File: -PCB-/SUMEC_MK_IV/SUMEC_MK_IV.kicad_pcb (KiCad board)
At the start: 2 copper layers, 15 parts, among them U1 TPS62133, U2 ESP32-S3-WROOM-1, U3 ESP32-S3-WROOM-1

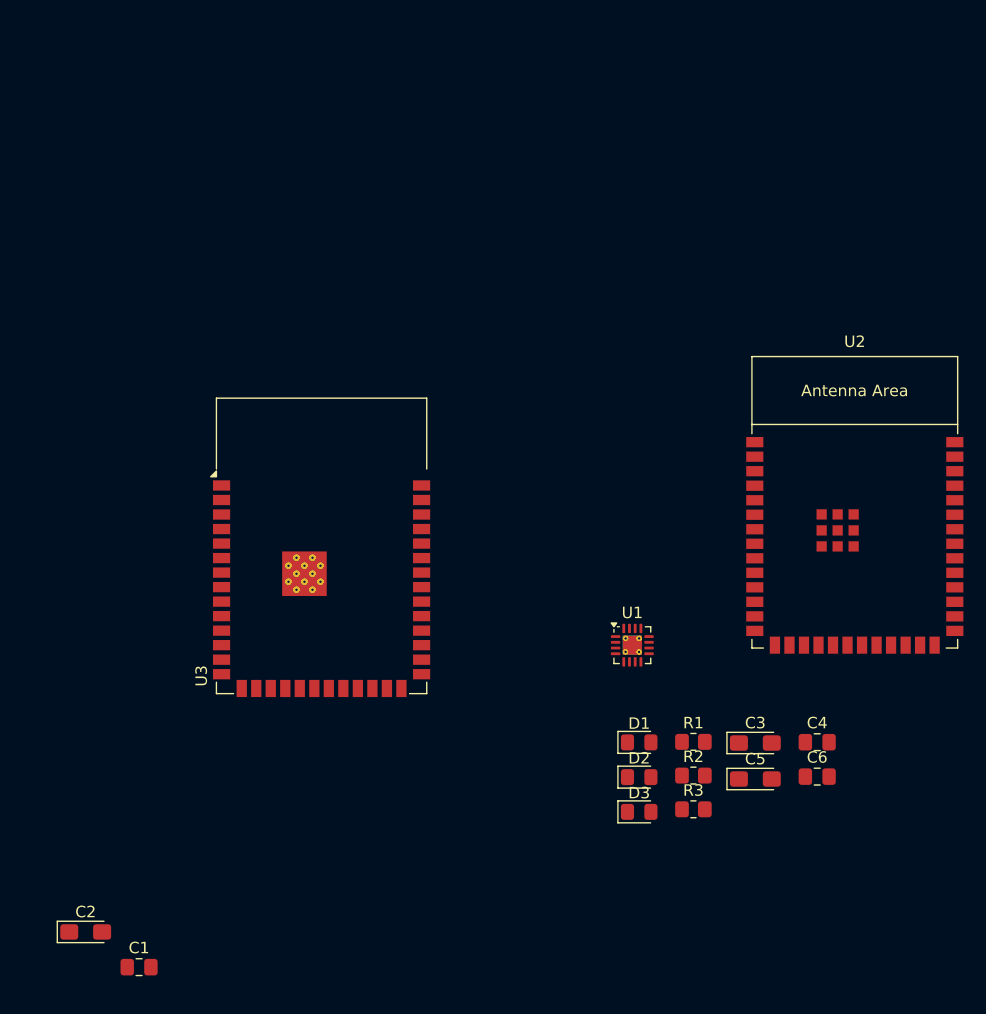
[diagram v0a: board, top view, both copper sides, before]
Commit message: VBATT VBUS Switching
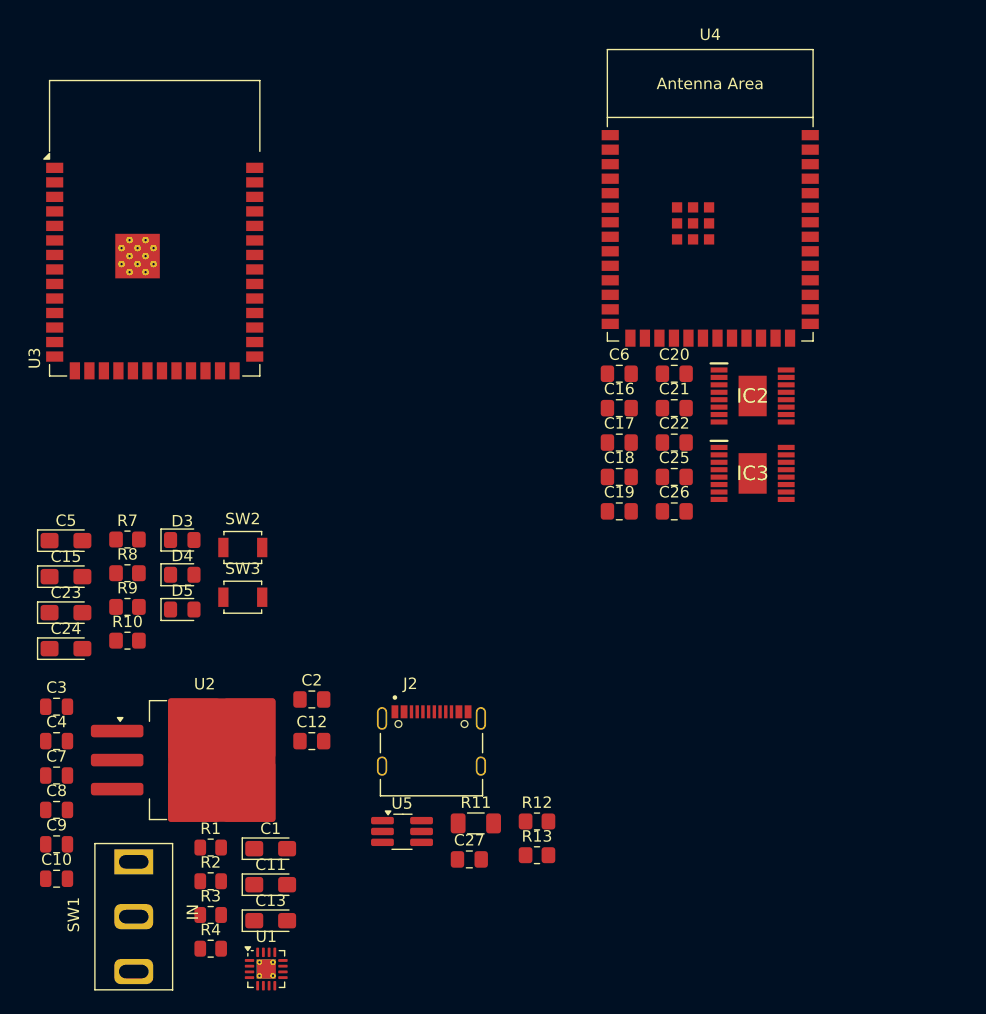
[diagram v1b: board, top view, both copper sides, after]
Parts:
- removed D1, D2: LED, LED_SMD:LED_0805_2012Metric_Pad1.15x1.40mm_HandSolder
- added C10: 100nF, Capacitor_SMD:C_0805_2012Metric, F.Cu at (111.7, 100.9)
- added C11: 10uF.stabl, Capacitor_Tantalum_SMD:CP_EIA-3216-18_Kemet-A_Pad1.58x1.35mm_HandSolder, F.Cu at (130.4, 101.5)
- added C12: 3.3nF, Capacitor_SMD:C_0805_2012Metric_Pad1.18x1.45mm_HandSolder, F.Cu at (134.0, 88.9)
- added C13: 10uF.stabl, Capacitor_Tantalum_SMD:CP_EIA-3216-18_Kemet-A_Pad1.58x1.35mm_HandSolder, F.Cu at (130.4, 104.6)
- added C15: 10uF.mcu, Capacitor_Tantalum_SMD:CP_EIA-3216-18_Kemet-A_Pad1.58x1.35mm_HandSolder, F.Cu at (112.5, 74.5)
- added C16: 100nF.mcu, Capacitor_SMD:C_0805_2012Metric_Pad1.18x1.45mm_HandSolder, F.Cu at (160.9, 59.8)
- added C17: 22nF.hb, Capacitor_SMD:C_0805_2012Metric_Pad1.18x1.45mm_HandSolder, F.Cu at (160.9, 62.8)
- added C18: 22nF.hb, Capacitor_SMD:C_0805_2012Metric_Pad1.18x1.45mm_HandSolder, F.Cu at (160.9, 65.8)
- added C19: 100nF, Capacitor_SMD:C_0805_2012Metric_Pad1.18x1.45mm_HandSolder, F.Cu at (160.9, 68.8)
- added C20: 100nF, Capacitor_SMD:C_0805_2012Metric_Pad1.18x1.45mm_HandSolder, F.Cu at (165.7, 56.8)
- added C21: 100nF.hb, Capacitor_SMD:C_0805_2012Metric_Pad1.18x1.45mm_HandSolder, F.Cu at (165.7, 59.8)
- added C22: 100nF.hb, Capacitor_SMD:C_0805_2012Metric_Pad1.18x1.45mm_HandSolder, F.Cu at (165.7, 62.8)
- added C23: 10uF.hb, Capacitor_Tantalum_SMD:CP_EIA-3216-18_Kemet-A_Pad1.58x1.35mm_HandSolder, F.Cu at (112.5, 77.7)
- added C24: 10uF.hb, Capacitor_Tantalum_SMD:CP_EIA-3216-18_Kemet-A_Pad1.58x1.35mm_HandSolder, F.Cu at (112.5, 80.8)
- added C25: 100nF.en, Capacitor_SMD:C_0805_2012Metric_Pad1.18x1.45mm_HandSolder, F.Cu at (165.7, 65.8)
- added C26: 100nF.boot, Capacitor_SMD:C_0805_2012Metric_Pad1.18x1.45mm_HandSolder, F.Cu at (165.7, 68.8)
- added C27: 100nF, Capacitor_SMD:C_0805_2012Metric_Pad1.18x1.45mm_HandSolder, F.Cu at (147.8, 99.2)
- added C7: 22uF, Capacitor_SMD:C_0805_2012Metric, F.Cu at (111.7, 91.9)
- added C8: 22uF, Capacitor_SMD:C_0805_2012Metric, F.Cu at (111.7, 94.9)
- added C9: 22uF, Capacitor_SMD:C_0805_2012Metric, F.Cu at (111.7, 97.9)
- added D4: LED, LED_SMD:LED_0805_2012Metric_Pad1.15x1.40mm_HandSolder, F.Cu at (122.7, 74.3)
- added D5: LED, LED_SMD:LED_0805_2012Metric_Pad1.15x1.40mm_HandSolder, F.Cu at (122.7, 77.4)
- added IC2: DRV8874PWPR, sumec-smdV2_library:DRV8874, F.Cu at (172.6, 58.7)
- added IC3: DRV8874PWPR, sumec-smdV2_library:DRV8874, F.Cu at (172.6, 65.5)
- added J2: TYPE-C-31-M-12, sumec-smdV2_library:USB_Type_C, F.Cu at (144.5, 91.1)
- added R10: 10k.mcu, Resistor_SMD:R_0805_2012Metric_Pad1.20x1.40mm_HandSolder, F.Cu at (117.9, 80.1)
- added R11: 0R, Resistor_SMD:R_1206_3216Metric_Pad1.30x1.75mm_HandSolder, F.Cu at (148.3, 96.1)
- added R12: 15R, Resistor_SMD:R_0805_2012Metric_Pad1.20x1.40mm_HandSolder, F.Cu at (153.7, 95.9)
- added R13: 15R, Resistor_SMD:R_0805_2012Metric_Pad1.20x1.40mm_HandSolder, F.Cu at (153.7, 98.9)
- added R4: 33k, Resistor_SMD:R_0805_2012Metric, F.Cu at (125.1, 107.1)
- added R7: 100R, Resistor_SMD:R_0805_2012Metric_Pad1.20x1.40mm_HandSolder, F.Cu at (117.9, 71.3)
- added R8: 100R, Resistor_SMD:R_0805_2012Metric_Pad1.20x1.40mm_HandSolder, F.Cu at (117.9, 74.2)
- added R9: 560R, Resistor_SMD:R_0805_2012Metric_Pad1.20x1.40mm_HandSolder, F.Cu at (117.9, 77.2)
- added SW1: SW_DPDT_x2, sumec-smdV2_library:Custom_SPDT_4.8mm_Switch, F.Cu at (118.4, 104.2)
- added SW2: SW_Push, Button_Switch_SMD:SW_SPST_B3U-1000P, F.Cu at (128.0, 72.0)
- added SW3: SW_Push, Button_Switch_SMD:SW_SPST_B3U-1000P, F.Cu at (128.0, 76.3)
- added U4: ESP32-S3-WROOM-1, PCM_Espressif:ESP32-S3-WROOM-1, F.Cu at (168.9, 44.1)
- added U5: USBLC6-2SC6, Package_TO_SOT_SMD:TSOT-23-6_HandSoldering, F.Cu at (141.9, 96.8)
- C1: value 100nF.mcu -> 10uF.bck; footprint Capacitor_SMD:C_0805_2012Metric_Pad1.18x1.45mm_HandSolder -> Capacitor_Tantalum_SMD:CP_EIA-3216-18_Kemet-A_Pad1.58x1.35mm_HandSolder
- C2: value 10uF.mcu -> 100nF.bck; footprint Capacitor_Tantalum_SMD:CP_EIA-3216-18_Kemet-A_Pad1.58x1.35mm_HandSolder -> Capacitor_SMD:C_0805_2012Metric_Pad1.18x1.45mm_HandSolder
- C3: value 10uF.mcu -> 22uF; footprint Capacitor_Tantalum_SMD:CP_EIA-3216-18_Kemet-A_Pad1.58x1.35mm_HandSolder -> Capacitor_SMD:C_0805_2012Metric
- C4: value 100nF.mcu -> 100nF; footprint Capacitor_SMD:C_0805_2012Metric_Pad1.18x1.45mm_HandSolder -> Capacitor_SMD:C_0805_2012Metric
- R1: value 100R -> 100k; footprint Resistor_SMD:R_0805_2012Metric_Pad1.20x1.40mm_HandSolder -> Resistor_SMD:R_0805_2012Metric
- R2: value 100R -> 22k; footprint Resistor_SMD:R_0805_2012Metric_Pad1.20x1.40mm_HandSolder -> Resistor_SMD:R_0805_2012Metric
- R3: value 560R -> 150k; footprint Resistor_SMD:R_0805_2012Metric_Pad1.20x1.40mm_HandSolder -> Resistor_SMD:R_0805_2012Metric
- U2: value ESP32-S3-WROOM-1 -> LM1084-3.3; footprint PCM_Espressif:ESP32-S3-WROOM-1 -> Package_TO_SOT_SMD:TO-263-3_TabPin2
- moved C4 66.5 mm to (111.7, 88.9)
- moved C5 63.8 mm to (112.5, 71.4)
- moved C3 61.2 mm to (111.7, 85.9)
- moved U2 60.2 mm to (124.6, 90.6)
- moved D3 46.5 mm to (122.7, 71.3)
- moved R1 43.2 mm to (125.1, 98.2)
- moved R2 43.2 mm to (125.1, 101.2)
- moved R3 43.2 mm to (125.1, 104.1)
- moved U1 42.8 mm to (130.0, 108.8)
- moved C6 39.3 mm to (160.9, 56.8)
- moved U3 31.4 mm to (120.2, 44.0)
- moved C2 28.4 mm to (134.0, 85.2)
- moved C1 15.5 mm to (130.4, 98.3)
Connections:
- C1 pad 1: unconnected-(C1-Pad1) -> +12V
- C1 pad 2: unconnected-(C1-Pad2) -> GND
- C2 pad 1: unconnected-(C2-Pad1) -> +12V
- C2 pad 2: unconnected-(C2-Pad2) -> GND
- C3 pad 1: +3V3 -> +BATT
- C4 pad 1: +3V3 -> +BATT
- D3 pad 2: +12V -> LED1
- R1 pad 1: Net-(D1-K) -> +BATT
- R1 pad 2: GND -> /POWER_SUPPLY/En_3V3
- R2 pad 1: Net-(D2-K) -> /POWER_SUPPLY/En_3V3
- R3 pad 1: Net-(D3-K) -> VCC
- R3 pad 2: GND -> Net-(IC1-FB)
- U1 pad 10: Net-(U1-VIN-Pad10) -> +12V
- U1 pad 11: Net-(U1-VIN-Pad10) -> +12V
- U1 pad 12: Net-(U1-VIN-Pad10) -> +12V
- U1 pad 13: unconnected-(U1-EN-Pad13) -> +12V
- U1 pad 14: unconnected-(U1-VOS-Pad14) -> VOUT 5V
- U1 pad 15: Net-(U1-GND-Pad15) -> GND
- U1 pad 16: Net-(U1-GND-Pad15) -> GND
- U1 pad 17: Net-(U1-GND-Pad15) -> GND
- U1 pad 4: unconnected-(U1-PG-Pad4) -> Net-(U1-PG)
- U1 pad 5: unconnected-(U1-FB-Pad5) -> GND
- U1 pad 6: Net-(U1-GND-Pad15) -> GND
- U1 pad 7: unconnected-(U1-FSW-Pad7) -> GND
- U1 pad 8: unconnected-(U1-DEF-Pad8) -> GND
- U1 pad 9: unconnected-(U1-SS/TR-Pad9) -> Net-(U1-SS/TR)
- U2 pad 3: EN -> +5V

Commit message: MK_IV update
Power supp sheet done, mechanical sheet almost done, some changes, updates etc.
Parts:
- added C28: 10uF.shrp, Capacitor_Tantalum_SMD:CP_EIA-3216-18_Kemet-A_Pad1.58x1.35mm_HandSolder, F.Cu at (149.8, 85.1)
- added C29: 10uF.shrp, Capacitor_Tantalum_SMD:CP_EIA-3216-18_Kemet-A_Pad1.58x1.35mm_HandSolder, F.Cu at (149.8, 88.3)
- added H1: Mounting Hole M3, MountingHole:MountingHole_3.2mm_M3_Pad_Via, F.Cu at (126.8, 66.7)
- added H2: Mounting Hole M3, MountingHole:MountingHole_3.2mm_M3_Pad_Via, F.Cu at (126.8, 74.6)
- added H3: Mounting Hole M3, MountingHole:MountingHole_3.2mm_M3_Pad_Via, F.Cu at (126.8, 82.6)
- added H4: Mounting Hole M3, MountingHole:MountingHole_3.2mm_M3_Pad_Via, F.Cu at (126.8, 90.5)
- added J3: Conn_01x06_Pin, Connector_Molex:Molex_PicoBlade_53398-0671_1x06-1MP_P1.25mm_Vertical, F.Cu at (149.9, 65.6)
- added J4: Conn_01x06_Pin, Connector_Molex:Molex_PicoBlade_53398-0671_1x06-1MP_P1.25mm_Vertical, F.Cu at (149.9, 72.6)
- added J5: Conn_01x06_Pin, Connector_Molex:Molex_PicoBlade_53398-0671_1x06-1MP_P1.25mm_Vertical, F.Cu at (149.9, 79.5)
- added J6: Conn_01x03_Pin, Connector_Molex:Molex_PicoBlade_53398-0371_1x03-1MP_P1.25mm_Vertical, F.Cu at (163.6, 65.6)
- added J7: Conn_01x03_Pin, Connector_Molex:Molex_PicoBlade_53398-0371_1x03-1MP_P1.25mm_Vertical, F.Cu at (163.6, 72.6)
- added J8: Conn_01x04_Pin, Connector_Molex:Molex_PicoBlade_53398-0471_1x04-1MP_P1.25mm_Vertical, F.Cu at (164.2, 86.5)
- added J9: Conn_01x03_Pin, Connector_Molex:Molex_PicoBlade_53398-0371_1x03-1MP_P1.25mm_Vertical, F.Cu at (163.6, 79.5)
- added R14: 10k, Resistor_SMD:R_0805_2012Metric_Pad1.20x1.40mm_HandSolder, F.Cu at (155.2, 85.0)
- added R15: 100, Resistor_SMD:R_0805_2012Metric_Pad1.20x1.40mm_HandSolder, F.Cu at (155.2, 88.0)
- added R16: R, sumec-remote_library:purosidenegative, F.Cu at (74.4, 34.7)
- added R17: R, sumec-smdV2_library:SPS LOGO, F.Cu at (201.8, -44.1)
- added R18: R, sumec-remote_library:boi, F.Cu at (107.1, 29.8)
- added R19: R, sumec-smdV2_library:Logo, F.Cu at (143.9, 17.3)
- added SW4: SW_Push, Button_Switch_SMD:SW_SPST_B3U-1000P, F.Cu at (133.7, 73.6)
- added SW5: SW_Push, Button_Switch_SMD:SW_SPST_B3U-1000P, F.Cu at (133.7, 77.9)
- added SW6: SW_Push, Button_Switch_SMD:SW_SPST_B3U-1000P, F.Cu at (133.7, 82.3)
- added TP1: TestPoint, TestPoint:TestPoint_Pad_D1.5mm, F.Cu at (138.4, 64.5)
- added TP2: TestPoint, TestPoint:TestPoint_Pad_D1.5mm, F.Cu at (138.4, 68.0)
- added TP3: TestPoint, TestPoint:TestPoint_Pad_D1.5mm, F.Cu at (138.4, 71.6)
- added TP4: TestPoint, TestPoint:TestPoint_Pad_D1.5mm, F.Cu at (138.4, 75.1)
- added U6: TSOP382xx, sumec-smdV2_library:TSOP, F.Cu at (144.5, 85.9)
- C11, C13: value 10uF.stabl -> 10uF.reg
- C2: value 100nF.bck -> 100nF.avin
- moved C23 92.2 mm to (204.7, 77.8)
- moved C24 92.2 mm to (204.7, 81.0)
- moved C27 81.9 mm to (226.7, 77.6)
- moved J2 81.9 mm to (223.4, 69.4)
- moved R11 81.9 mm to (227.3, 74.4)
- moved R12 81.9 mm to (232.7, 74.3)
- moved R13 81.9 mm to (232.7, 77.2)
- moved U5 81.9 mm to (220.8, 75.1)
- moved U4 68.2 mm to (110.5, 79.3)
- moved C1 66.9 mm to (193.6, 76.6)
- moved C10 66.9 mm to (174.9, 79.3)
- moved C11 66.9 mm to (193.6, 79.8)
- moved C13 66.9 mm to (193.6, 82.9)
- moved C3 66.9 mm to (174.9, 64.2)
- moved C4 66.9 mm to (174.9, 67.2)
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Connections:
- net OUT 1A renamed M1A
- net OUT 1B renamed M1B
- net OUT 2A renamed M2A
- net OUT 2B renamed M2B
- C5 pad 1: Net-(U3-3V3) -> +3V3
- C6 pad 1: Net-(U3-3V3) -> +3V3
- U3 pad 13: unconnected-(U3-IO19-Pad13) -> D-
- U3 pad 14: unconnected-(U3-IO20-Pad14) -> D+
- U3 pad 2: Net-(U3-3V3) -> +3V3

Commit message: MKIV major update
Updated everything, custom symbol for ESP32, MCU sheet done, new test points added, motor control revision.

all left is to clean it up a bit
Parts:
- removed C17, C18: 22nF.hb, Capacitor_SMD:C_0805_2012Metric_Pad1.18x1.45mm_HandSolder
- removed C19, C20: 100nF, Capacitor_SMD:C_0805_2012Metric_Pad1.18x1.45mm_HandSolder
- added D7: LED, LED_SMD:LED_0805_2012Metric_Pad1.15x1.40mm_HandSolder, F.Cu at (91.5, 144.8)
- added R26: 0R, Resistor_SMD:R_1206_3216Metric_Pad1.30x1.75mm_HandSolder, F.Cu at (202.5, 108.1)
- added R27: 0R, Resistor_SMD:R_1206_3216Metric_Pad1.30x1.75mm_HandSolder, F.Cu at (202.5, 111.4)
- added R28: 0R, Resistor_SMD:R_1206_3216Metric_Pad1.30x1.75mm_HandSolder, F.Cu at (202.5, 114.7)
- added R29: 0R, Resistor_SMD:R_1206_3216Metric_Pad1.30x1.75mm_HandSolder, F.Cu at (202.5, 118.0)
- added R30: 100R, Resistor_SMD:R_0805_2012Metric_Pad1.20x1.40mm_HandSolder, F.Cu at (96.2, 144.5)
- added TP5: TestPoint, TestPoint:TestPoint_Pad_D1.5mm, F.Cu at (127.4, 118.9)
- added TP6: TestPoint, TestPoint:TestPoint_Pad_D1.5mm, F.Cu at (127.4, 122.4)
- J4: value Conn_01x06_Pin -> Conn_01x03_Pin; footprint Connector_Molex:Molex_PicoBlade_53398-0671_1x06-1MP_P1.25mm_Vertical -> Connector_Molex:Molex_PicoBlade_53398-0371_1x03-1MP_P1.25mm_Vertical
- J7: value Conn_01x03_Pin -> Conn_01x06_Pin; footprint Connector_Molex:Molex_PicoBlade_53398-0371_1x03-1MP_P1.25mm_Vertical -> Connector_Molex:Molex_PicoBlade_53398-0671_1x06-1MP_P1.25mm_Vertical
- TP1: footprint TestPoint:TestPoint_Pad_D1.5mm -> TestPoint:TestPoint_Loop_D1.80mm_Drill1.0mm_Beaded
- moved U2 96.6 mm to (138.7, 152.0)
- moved TP1 67.1 mm to (126.9, 130.5)
- moved J7 56.4 mm to (138.9, 123.3)
- moved R19 54.1 mm to (107.9, 57.8)
- moved J6 51.9 mm to (152.6, 116.3)
- moved C21 49.4 mm to (193.1, 121.5)
- moved C22 49.4 mm to (193.1, 124.5)
- moved C16 45.1 mm to (107.1, 138.7)
- moved C26 45.1 mm to (122.1, 132.7)
- moved D3 45.1 mm to (91.5, 135.7)
- moved R8 45.1 mm to (96.2, 138.6)
- moved H1 45.1 mm to (115.8, 110.4)
- moved H2 45.1 mm to (115.8, 118.4)
- moved H3 45.1 mm to (115.8, 126.3)
- moved R10 45.1 mm to (122.1, 135.7)
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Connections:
- C3 pad 1: +BATT -> +5V
- C4 pad 1: +BATT -> +5V
- IC2 pad 16: GND -> Net-(IC2-PMODE)
- IC2 pad 4: unconnected-(IC2-NFAULT-Pad4) -> nFAULT
- IC2 pad 5: unconnected-(IC2-VREF-Pad5) -> +3V3
- IC2 pad 6: unconnected-(IC2-IPROPI-Pad6) -> IPROPI_ADC
- IC2 pad 7: unconnected-(IC2-IMODE-Pad7) -> Net-(IC2-IMODE)
- IC3 pad 16: GND -> Net-(IC3-PMODE)
- IC3 pad 4: unconnected-(IC3-NFAULT-Pad4) -> nFAULT
- IC3 pad 5: unconnected-(IC3-VREF-Pad5) -> +3V3
- IC3 pad 6: unconnected-(IC3-IPROPI-Pad6) -> IPROPI_ADC
- IC3 pad 7: unconnected-(IC3-IMODE-Pad7) -> Net-(IC3-IMODE)
- J4 pad 1: +5V -> SHARP 1
- J4 pad 2: SDA -> +3V3
- J4 pad 3: SCL -> GND
- J6 pad 1: SHARP 1 -> SHARP 2
- J7 pad 1: SHARP 2 -> +5V
- J7 pad 2: +3V3 -> SDA
- J7 pad 3: GND -> SCL
- R1 pad 1: +BATT -> +5V
- TP1 pad 1: unconnected-(TP1-Pad1) -> +3V3
- TP2 pad 1: unconnected-(TP2-Pad1) -> SCL
- TP3 pad 1: unconnected-(TP3-Pad1) -> SDA
- TP4 pad 1: unconnected-(TP4-Pad1) -> D-
- U3 pad 10: unconnected-(U3-IO17-Pad10) -> SCL
- U3 pad 11: unconnected-(U3-IO18-Pad11) -> SDA
- U3 pad 12: unconnected-(U3-IO8-Pad12) -> OUT 1B
- U3 pad 17: unconnected-(U3-IO9-Pad17) -> POL 2
- U3 pad 18: unconnected-(U3-IO10-Pad18) -> LED3
- U3 pad 22: unconnected-(U3-IO14-Pad22) -> POL 1
- U3 pad 23: unconnected-(U3-IO21-Pad23) -> IR MODULE
- U3 pad 24: unconnected-(U3-IO47-Pad24) -> LED1
- U3 pad 25: unconnected-(U3-IO48-Pad25) -> LED2
- U3 pad 27: unconnected-(U3-IO0-Pad27) -> BOOT
- U3 pad 28: unconnected-(U3-IO35-Pad28) -> PWM1
- U3 pad 29: unconnected-(U3-IO36-Pad29) -> PWM2
- U3 pad 3: unconnected-(U3-EN-Pad3) -> EN
- U3 pad 30: unconnected-(U3-IO37-Pad30) -> IN1
- U3 pad 31: unconnected-(U3-IO38-Pad31) -> IN2
- U3 pad 32: unconnected-(U3-IO39-Pad32) -> nSLEEP
- U3 pad 33: unconnected-(U3-IO40-Pad33) -> nFAULT
- U3 pad 34: unconnected-(U3-IO41-Pad34) -> SHARP 2
- U3 pad 35: unconnected-(U3-IO42-Pad35) -> SHARP 1
- U3 pad 38: unconnected-(U3-IO2-Pad38) -> POL 3
- U3 pad 39: unconnected-(U3-IO1-Pad39) -> IPROPI_ADC
- U3 pad 4: unconnected-(U3-IO4-Pad4) -> QRE1113 B
- U3 pad 5: unconnected-(U3-IO5-Pad5) -> QRE1113 A
- U3 pad 6: unconnected-(U3-IO6-Pad6) -> QRE1113 C
- U3 pad 7: unconnected-(U3-IO7-Pad7) -> OUT 1A
- U3 pad 8: unconnected-(U3-IO15-Pad8) -> OUT 2A
- U3 pad 9: unconnected-(U3-IO16-Pad9) -> OUT 2B
- U4 pad 12: QRE1113 C -> unconnected-(U4-GPIO8/TOUCH8/ADC1_CH7/SUBSPICS1-Pad12)
- U4 pad 17: QRE1113 A -> unconnected-(U4-GPIO9/TOUCH9/ADC1_CH8/FSPIHD/SUBSPIHD-Pad17)
- U4 pad 18: QRE1113 B -> unconnected-(U4-GPIO10/TOUCH10/ADC1_CH9/FSPICS0/FSPIIO4/SUBSPICS0-Pad18)
- U4 pad 28: SHARP 2 -> unconnected-(U4-SPIIO6/GPIO35/FSPID/SUBSPID-Pad28)
- U4 pad 31: IR MODULE -> unconnected-(U4-GPIO38/FSPIWP/SUBSPIWP-Pad31)
- U4 pad 38: TEST PROGRAM -> unconnected-(U4-GPIO2/TOUCH2/ADC1_CH1-Pad38)
- U4 pad 9: SHARP 1 -> unconnected-(U4-GPIO16/U0CTS/ADC2_CH5/XTAL_32K_N-Pad9)
